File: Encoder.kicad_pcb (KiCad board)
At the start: 2 copper layers, 23.5 x 19 mm, 12 parts, among them J1 Conn_01x05_Pin, SW1 RotaryEncoder_Switch_MP, U1 74LVC3G14

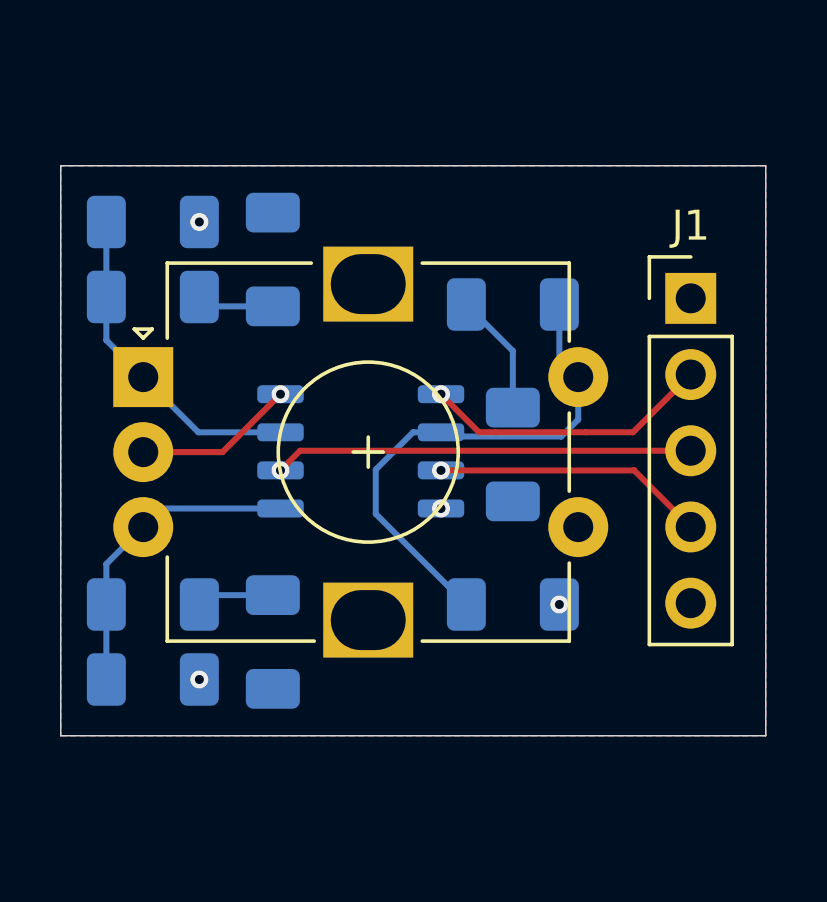
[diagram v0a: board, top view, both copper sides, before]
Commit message: Add mounting holes
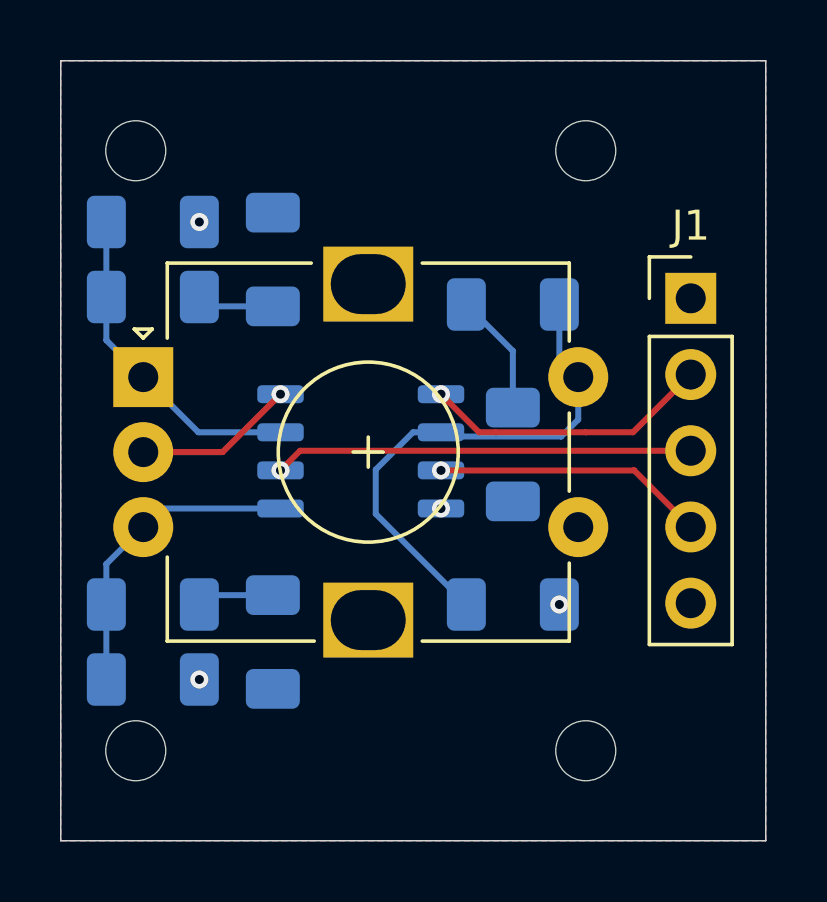
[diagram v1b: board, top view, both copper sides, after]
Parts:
- added H1: MountingHole, MountingHole:MountingHole_2mm, F.Cu at (134.0, 72.5)
- added H2: MountingHole, MountingHole:MountingHole_2mm, F.Cu at (134.0, 92.5)
- added H3: MountingHole, MountingHole:MountingHole_2mm, F.Cu at (119.0, 72.5)
- added H4: MountingHole, MountingHole:MountingHole_2mm, F.Cu at (119.0, 92.5)
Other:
- board size 23.5 x 19 mm -> 23.5 x 26 mm

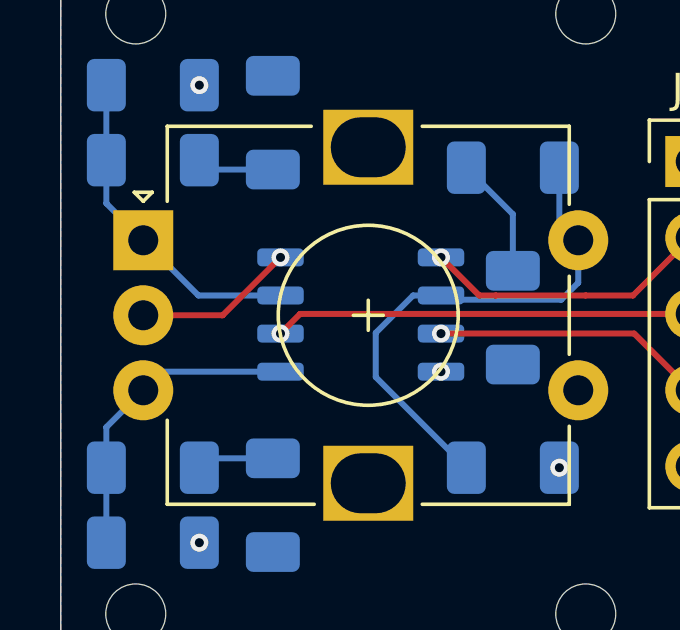
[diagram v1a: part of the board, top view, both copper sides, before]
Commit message: Add decoupling capacitor
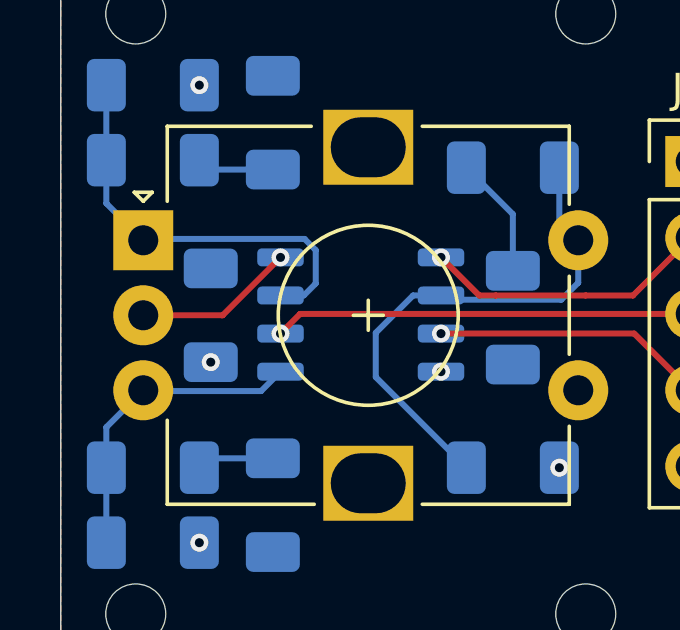
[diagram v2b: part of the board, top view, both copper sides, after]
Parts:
- added C4: 100n, Capacitor_SMD:C_1206_3216Metric_Pad1.33x1.80mm_HandSolder, B.Cu at (121.5, 82.5)
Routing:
- net /A: track 11.0 -> 14.1 mm
- net /B: track 10.4 -> 11.3 mm
- net VCC: vias 4 -> 5

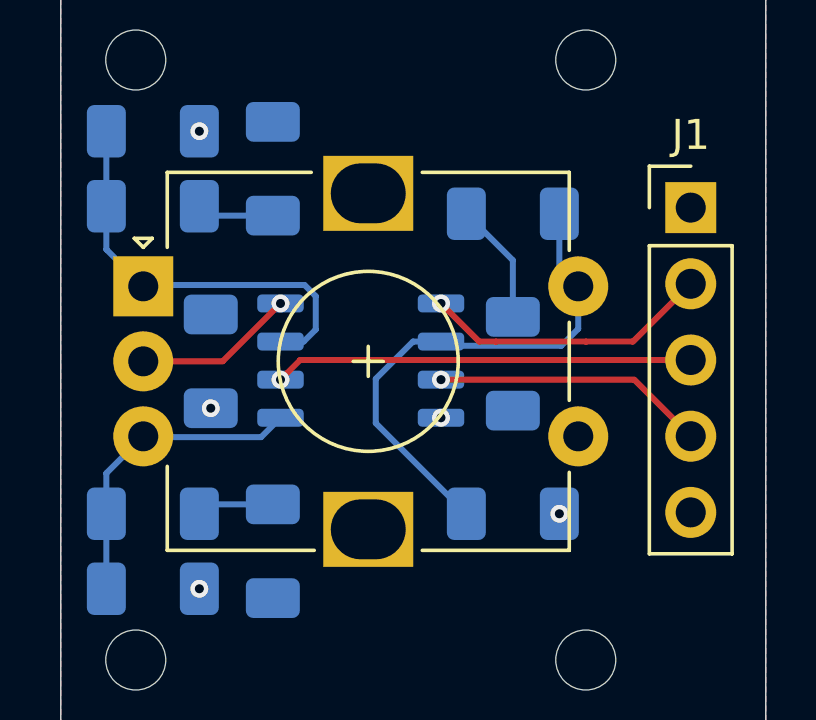
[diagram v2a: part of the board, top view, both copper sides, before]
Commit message: Fix debounce routing
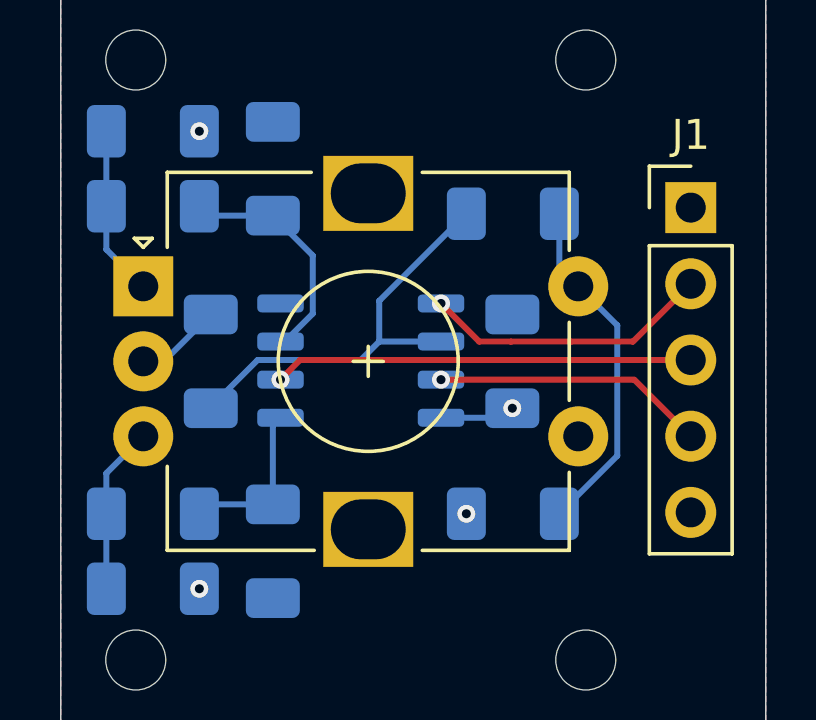
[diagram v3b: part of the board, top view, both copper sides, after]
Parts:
- moved C1 10.1 mm to (121.5, 82.5), turned to 90 degrees
- moved C4 10.1 mm to (131.6, 82.5)
- turned R1 to 0 degrees
- turned R2 to 180 degrees
- turned R3 to 0 degrees
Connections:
- R2 pad 1: Net-(C1-Pad1) -> /BTN
- R2 pad 2: /BTN -> Net-(C1-Pad1)
- R3 pad 1: Net-(C2-Pad1) -> /A
- R3 pad 2: /A -> Net-(C2-Pad1)
- U1 pad 1: /B -> Net-(C3-Pad1)
- U1 pad 3: /A -> Net-(C2-Pad1)
- U1 pad 6: /BTN -> Net-(C1-Pad1)
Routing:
- net Net-(C1-Pad1): track 4.08 -> 14.1 mm
- net /A: track 14.1 -> 5.68 mm
- net /BTN: track 17.4 -> 11.6 mm
- net /B: track 11.3 -> 5.59 mm
- net Net-(C2-Pad1): track 2.58 -> 7.86 mm
- net Net-(C3-Pad1): track 2.58 -> 5.57 mm
- net VCC: track 0.00 -> 2.51 mm, vias 5 -> 4
- net GND: track 5.37 -> 2.90 mm, vias 1 -> 0

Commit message: Layout done
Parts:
- U1: footprint Package_SO:SSOP-8_3.9x5.05mm_P1.27mm -> Package_SO:VSSOP-8_2.3x2mm_P0.5mm
- moved H3 55.9 mm to (145.0, 122.0)
- moved H2 41.5 mm to (163.2, 122.0)
- moved C1 41.2 mm to (153.5, 108.5), turned to 180 degrees
- moved H1 40.5 mm to (163.2, 100.5)
- moved R3 39.2 mm to (145.8, 106.5)
- moved R4 39.2 mm to (145.8, 104.0)
- moved R1 39.0 mm to (157.0, 117.2)
- moved C2 39.0 mm to (149.5, 105.2)
- moved U1 38.7 mm to (152.4, 111.2)
- moved R5 38.6 mm to (145.8, 116.0)
- moved R6 38.6 mm to (145.8, 118.5)
- moved J1 38.6 mm to (163.2, 106.2)
- moved SW1 38.6 mm to (145.0, 108.8)
- moved C3 38.4 mm to (149.5, 117.2)
- moved C4 38.4 mm to (153.5, 114.0), turned to 180 degrees
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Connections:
- SW1 pad S1: /BTN -> GND
- SW1 pad S2: GND -> /BTN
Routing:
- net Net-(C1-Pad1): track 14.1 -> 7.76 mm
- net /Debounced.B: track 9.11 -> 12.6 mm
- net GND: track 2.90 -> 0.00 mm
- net /Debounced.A: track 9.65 -> 12.1 mm
- net /BTN: track 11.6 -> 13.9 mm
- net /Debounced.BTN: track 13.9 -> 12.3 mm
- net Net-(C3-Pad1): track 5.57 -> 6.97 mm
- net VCC: track 2.51 -> 3.45 mm
- net /A: track 5.68 -> 5.08 mm
- net /B: track 5.59 -> 5.08 mm
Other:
- board size 23.5 x 26 mm -> 23.2 x 26.5 mm

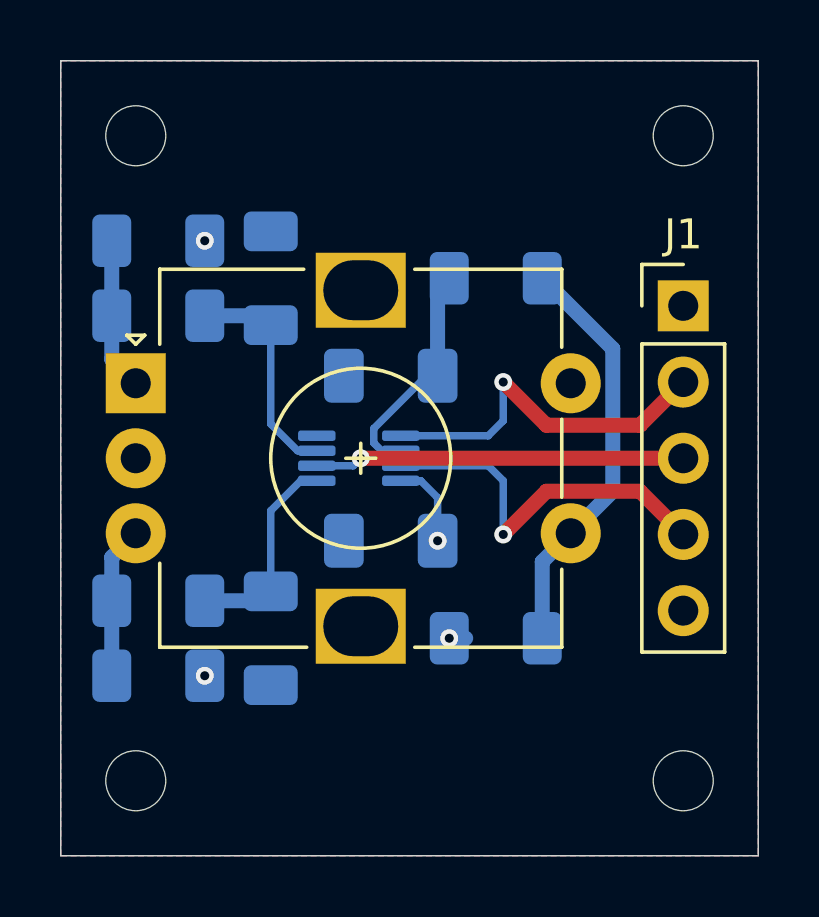
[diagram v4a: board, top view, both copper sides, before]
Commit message: Add header labels
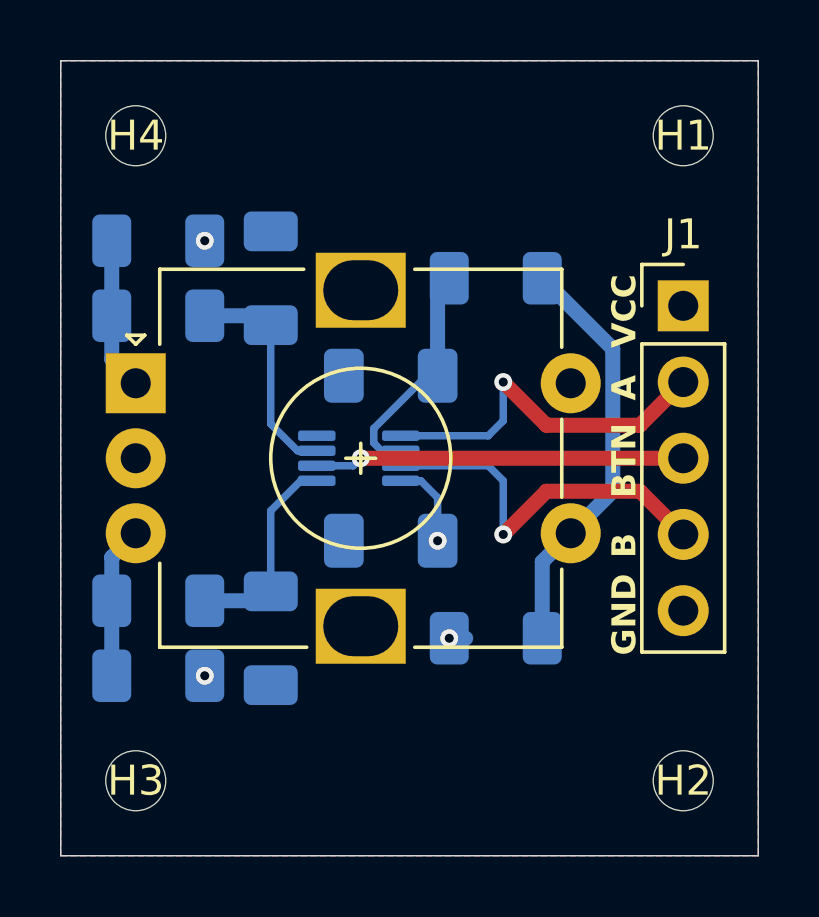
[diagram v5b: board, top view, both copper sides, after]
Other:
- board text added: "A"
- board text added: "B"
- board text added: "BTN"
- board text added: "GND"
- board text added: "VCC"

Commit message: Address warnings
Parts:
- moved C2 3.51 mm to (149.8, 108.8)
- moved C3 3.51 mm to (149.8, 113.8)
- moved R3 2.70 mm to (147.2, 108.8), turned to -90 degrees
- moved R5 2.70 mm to (147.2, 113.8), turned to -90 degrees
- moved R4 2.67 mm to (148.2, 105.0), turned to 0 degrees
- moved R6 2.67 mm to (148.2, 117.5), turned to 0 degrees
- moved U1 2.56 mm to (155.0, 111.2)
- moved C1 1.31 mm to (154.8, 108.5)
- moved C4 1.31 mm to (154.8, 114.0)
- moved H1 1.00 mm to (163.2, 101.5)
- moved H2 1.00 mm to (163.2, 121.0)
- moved H3 1.00 mm to (145.0, 121.0)
- moved H4 1.00 mm to (145.0, 101.5)
- moved R1 0.75 mm to (157.0, 116.5)
- moved R2 0.75 mm to (157.0, 106.0)
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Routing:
- net /Debounced.B: track 12.6 -> 8.30 mm
- net /Debounced.A: track 12.1 -> 7.92 mm
- net /Debounced.BTN: track 12.3 -> 9.75 mm
- net VCC: track 3.45 -> 2.01 mm
- net /BTN: track 13.9 -> 12.6 mm
- net /B: track 5.08 -> 6.37 mm
- net /A: track 5.08 -> 6.37 mm
- net Net-(C1-Pad1): track 7.76 -> 6.50 mm
- net Net-(C2-Pad1): track 7.53 -> 6.64 mm
- net Net-(C3-Pad1): track 6.97 -> 6.43 mm
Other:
- board size 23.2 x 26.5 mm -> 23.2 x 24 mm

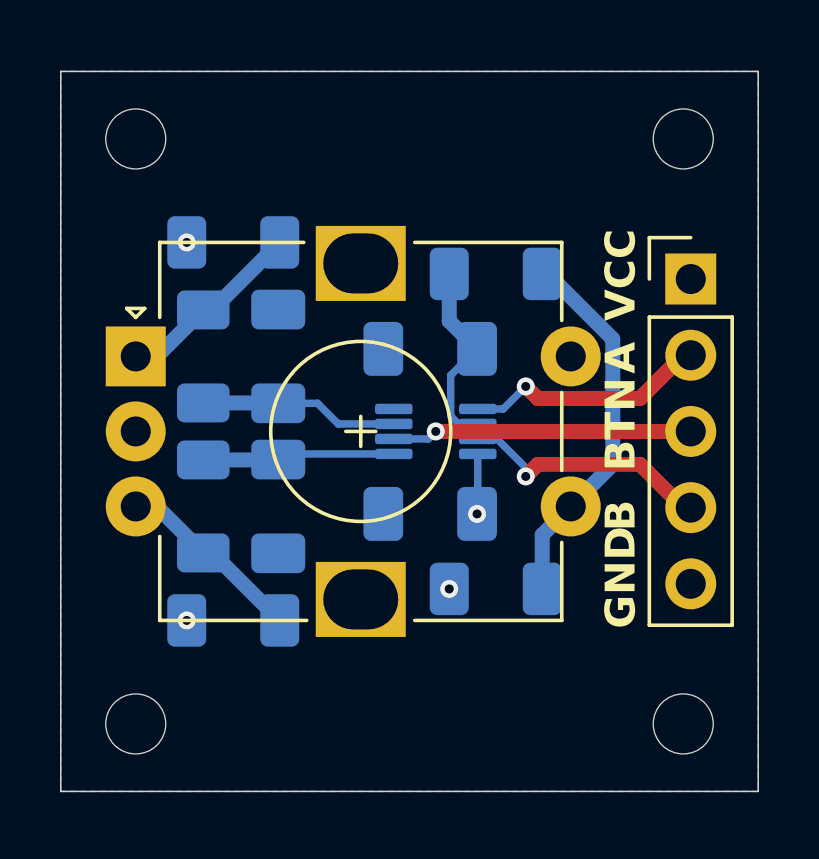
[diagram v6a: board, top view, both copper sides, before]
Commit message: Rounded PCB corners
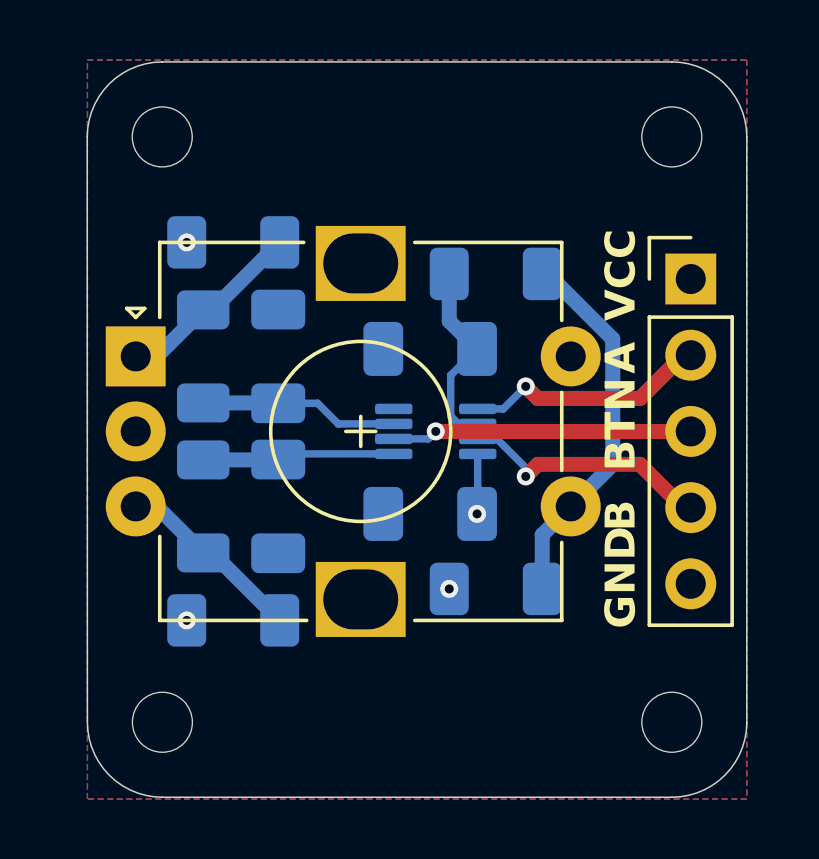
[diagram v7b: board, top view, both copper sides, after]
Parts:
- moved H3 0.89 mm to (145.9, 120.9)
- moved H4 0.89 mm to (145.9, 101.4)
- moved H1 0.39 mm to (162.9, 101.4)
- moved H2 0.39 mm to (162.9, 120.9)
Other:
- board size 23.2 x 24 mm -> 22 x 24.5 mm
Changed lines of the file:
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@@
 	(footprint "MountingHole:MountingHole_2mm"
 		(layer "F.Cu")
-		(at 163.25 101.5)
+		(at 162.869 101.433)
 		(descr "Mounting Hole 2mm, no annular, generated by kicad-footprint-generator mountinghole.py")
 		(tags "mountinghole")
@@
 	(footprint "MountingHole:MountingHole_2mm"
 		(layer "F.Cu")
-		(at 145 101.5)
+		(at 145.883 101.433)
 		(descr "Mounting Hole 2mm, no annular, generated by kicad-footprint-generator mountinghole.py")
 		(tags "mountinghole")
@@
 	(footprint "MountingHole:MountingHole_2mm"
 		(layer "F.Cu")
-		(at 145 121)
+		(at 145.888297 120.944)
 		(descr "Mounting Hole 2mm, no annular, generated by kicad-footprint-generator mountinghole.py")
 		(tags "mountinghole")
@@
 	(footprint "MountingHole:MountingHole_2mm"
 		(layer "F.Cu")
-		(at 163.25 121)
+		(at 162.869 120.944)
 		(descr "Mounting Hole 2mm, no annular, generated by kicad-footprint-generator mountinghole.py")
 		(tags "mountinghole")
@@
 		)
 	)
-	(gr_rect
-		(start 142.5 99.25)
-		(end 165.75 123.25)
+	(gr_arc
+		(start 165.369 120.944)
+		(mid 164.636767 122.711767)
+		(end 162.869 123.444)
 		(stroke
 			(width 0.05)
-			(type default)
+			(type solid)
+		)
+		(layer "Edge.Cuts")
+	)
+	(gr_line
+		(start 162.869 123.444)
+		(end 145.888297 123.444)
+		(stroke
+			(width 0.05)
+			(type solid)
+		)
+		(layer "Edge.Cuts")
+	)
+	(gr_line
+		(start 143.388328 120.944)
+		(end 143.383077 101.433)
+		(stroke
+			(width 0.05)
+			(type solid)
+		)
+		(layer "Edge.Cuts")
+	)
+	(gr_arc
+		(start 162.869 98.933)
+		(mid 164.636767 99.665233)
+		(end 165.369 101.433)
+		(stroke
+			(width 0.05)
+			(type solid)
+		)
+		(layer "Edge.Cuts")
+	)
+	(gr_line
+		(start 145.883 98.933)
+		(end 162.869 98.933)
+		(stroke
+			(width 0.05)
+			(type solid)
+		)
+		(layer "Edge.Cuts")
+	)
+	(gr_arc
+		(start 145.888297 123.444)
+		(mid 144.12053 122.711767)
+		(end 143.388297 120.944)
+		(stroke
+			(width 0.05)
+			(type solid)
+		)
+		(layer "Edge.Cuts")
+	)
+	(gr_line
+		(start 165.369 101.433)
+		(end 165.369 120.944)
+		(stroke
+			(width 0.05)
+			(type solid)
+		)
+		(layer "Edge.Cuts")
+	)
+	(gr_arc
+		(start 143.383 101.433)
+		(mid 144.115233 99.665233)
+		(end 145.883 98.933)
+		(stroke
+			(width 0.05)
+			(type solid)
 		)
-		(fill no)
 		(layer "Edge.Cuts")
 	)
@@
 		(polygon
 			(pts
-				(xy 142.5 99.25) (xy 165.75 99.25) (xy 165.75 123.25) (xy 142.5 123.25)
+				(xy 143.389 98.869) (xy 165.369 98.869) (xy 165.369 123.504) (xy 143.389 123.504)
 			)
 		)
@@
 		(polygon
 			(pts
-				(xy 142.5 99.25) (xy 165.75 99.25) (xy 165.75 123.25) (xy 142.5 123.25)
+				(xy 143.389 98.869) (xy 165.369 98.869) (xy 165.369 123.504) (xy 143.389 123.504)
 			)
 		)

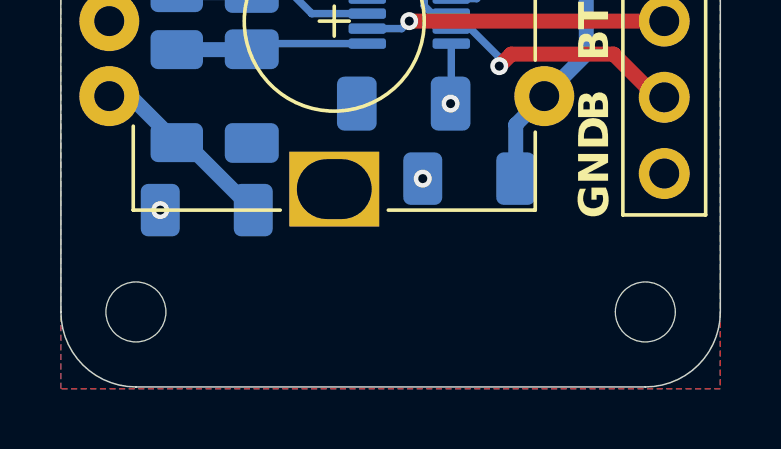
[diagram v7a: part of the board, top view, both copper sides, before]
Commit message: Add version to silkscreen
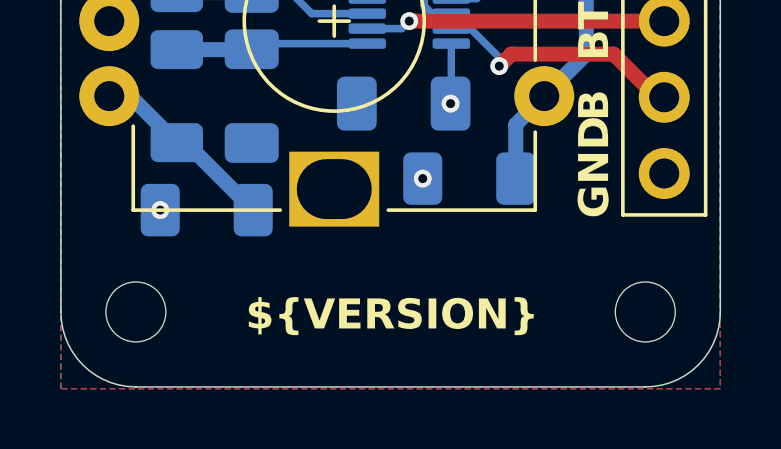
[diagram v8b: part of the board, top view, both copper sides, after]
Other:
- board text added: "${VERSION}"
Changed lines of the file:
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@@
 		)
 	)
+	(property "VERSION" "01.00")
 	(net 0 "")
 	(net 1 "GND")
@@
 		)
 	)
+	(gr_text "${VERSION}"
+		(at 154.432 121.031 0)
+		(layer "F.SilkS")
+		(effects
+			(font
+				(size 1 1)
+				(thickness 0.2)
+				(bold yes)
+			)
+		)
+	)
